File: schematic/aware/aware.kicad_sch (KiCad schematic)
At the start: 28 parts, among them J1 Servo_Conn, J2 Nowcast_LEDS_Conn, J3 Forcast_LEDS_Conn, J4 Battery_Conn, Q1 BC548, U1 Solar_Charger, U2 LM393

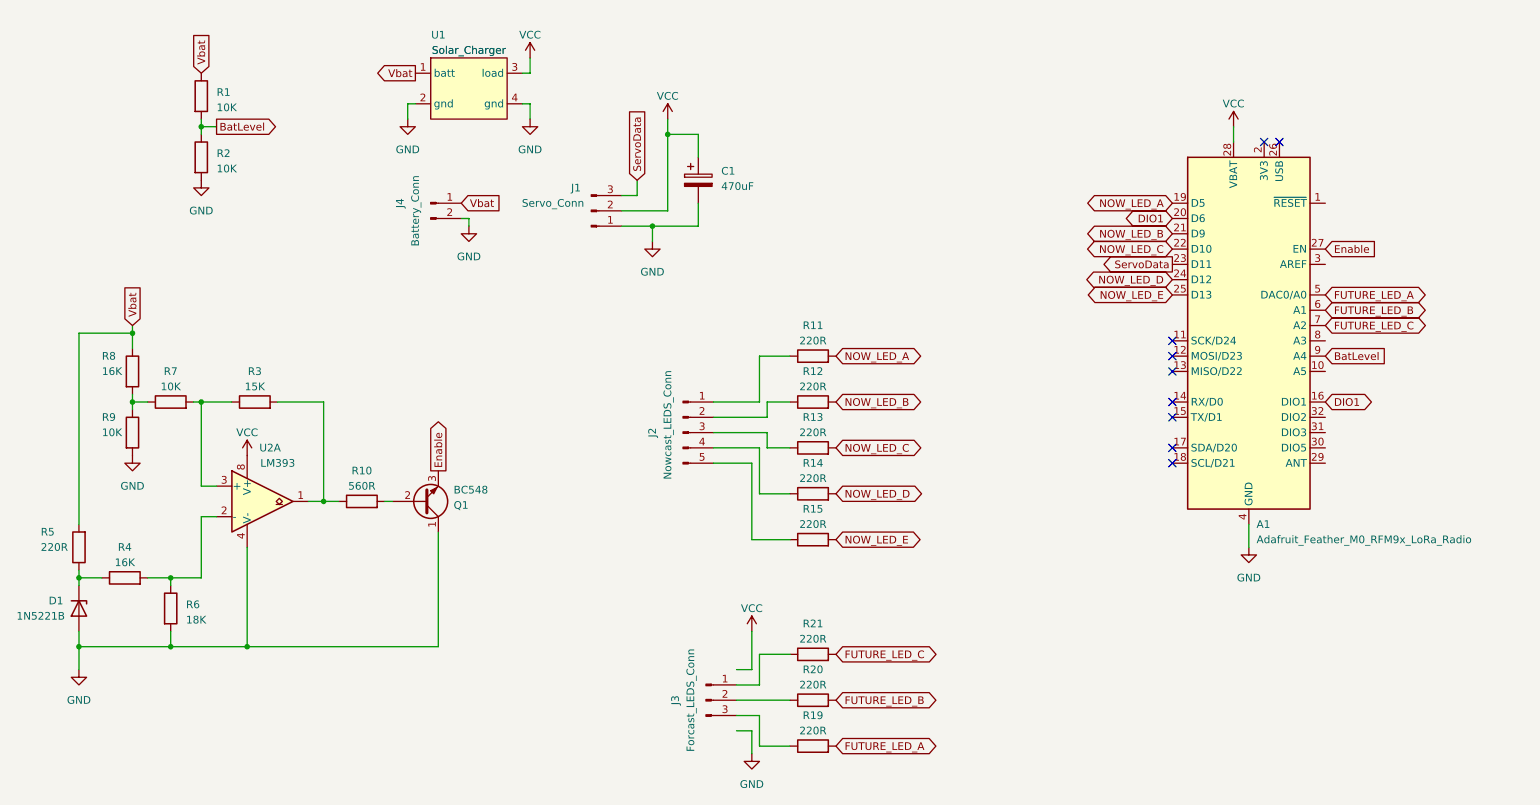
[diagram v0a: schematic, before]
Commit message: adjusted pinout of forcast connector on mainboard
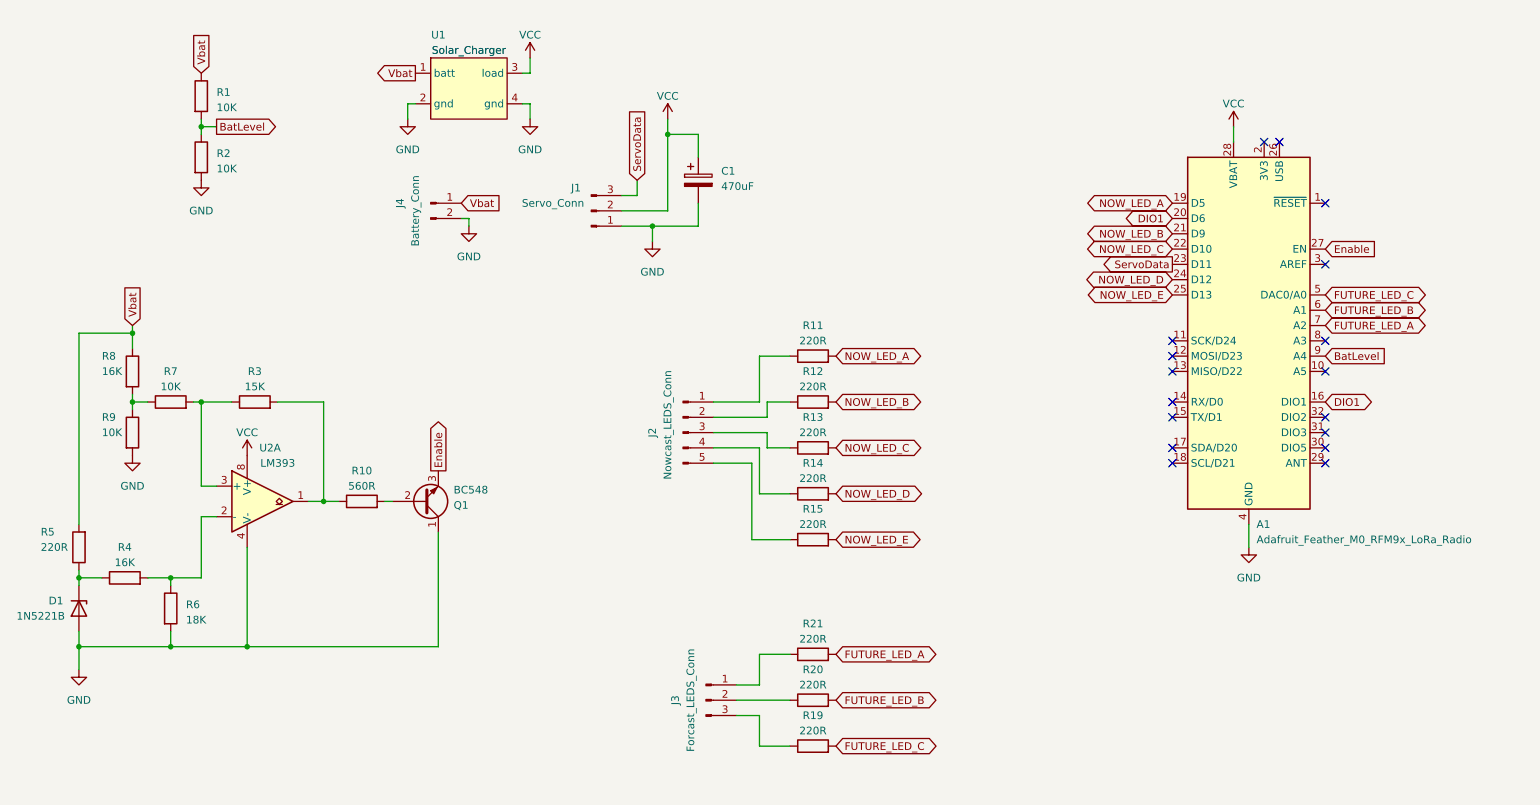
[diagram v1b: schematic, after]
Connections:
- net FUTURE_LED_A: now also A1.7 (A2), R21.2; no longer A1.5 (DAC0/A0), R19.2
- net FUTURE_LED_C: now also A1.5 (DAC0/A0), R19.2; no longer A1.7 (A2), R21.2
- no-connect marks 9 -> 17
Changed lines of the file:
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@@
   (no_connect (at 238.76 43.18))
   (no_connect (at 220.98 88.9))
+  (no_connect (at 246.38 53.34))
   (no_connect (at 236.22 43.18))
+  (no_connect (at 246.38 91.44))
+  (no_connect (at 246.38 96.52))
+  (no_connect (at 246.38 76.2))
   (no_connect (at 220.98 76.2))
   (no_connect (at 220.98 93.98))
   (no_connect (at 220.98 78.74))
+  (no_connect (at 246.38 93.98))
+  (no_connect (at 246.38 88.9))
   (no_connect (at 220.98 81.28))
+  (no_connect (at 246.38 81.28))
+  (no_connect (at 246.38 63.5))
   (wire (pts (xy 142.24 53.34) (xy 142.24 57.15))
     (stroke (width 0) (type default))
@@
     (stroke (width 0) (type default))
   )
-  (wire (pts (xy 151.13 130.81) (xy 151.13 124.46))
-    (stroke (width 0) (type default))
-  )
   (wire (pts (xy 54.61 124.46) (xy 54.61 127))
     (stroke (width 0) (type default))
@@
     (stroke (width 0) (type default))
   )
-  (wire (pts (xy 148.59 140.97) (xy 151.13 140.97))
-    (stroke (width 0) (type default))
-  )
   (wire (pts (xy 80.01 86.36) (xy 80.01 102.87))
     (stroke (width 0) (type default))
@@
     (stroke (width 0) (type default))
   )
-  (wire (pts (xy 148.59 130.81) (xy 151.13 130.81))
-    (stroke (width 0) (type default))
-  )
   (wire (pts (xy 48.26 74.93) (xy 48.26 77.47))
     (stroke (width 0) (type default))
@@
   )
   (wire (pts (xy 54.61 115.57) (xy 59.69 115.57))
-    (stroke (width 0) (type default))
-  )
-  (wire (pts (xy 151.13 140.97) (xy 151.13 144.78))
     (stroke (width 0) (type default))
   )
@@
     )
   )
-  (global_label "FUTURE_LED_A" (shape bidirectional) (at 165.1 143.51 0) (fields_autoplaced)
-    (effects (font (size 1.27 1.27)) (justify left))
-    (property "Intersheetrefs" "${INTERSHEET_REFS}" (at 181.9112 143.51 0)
-      (effects (font (size 1.27 1.27)) (justify left) hide)
-    )
-  )
-  (global_label "FUTURE_LED_A" (shape bidirectional) (at 246.38 68.58 0) (fields_autoplaced)
-    (effects (font (size 1.27 1.27)) (justify left))
-    (property "Intersheetrefs" "${INTERSHEET_REFS}" (at 263.1912 68.58 0)
+  (global_label "FUTURE_LED_A" (shape bidirectional) (at 165.1 128.27 0) (fields_autoplaced)
+    (effects (font (size 1.27 1.27)) (justify left))
+    (property "Intersheetrefs" "${INTERSHEET_REFS}" (at 181.9112 128.27 0)
+      (effects (font (size 1.27 1.27)) (justify left) hide)
+    )
+  )
+  (global_label "FUTURE_LED_A" (shape bidirectional) (at 246.38 73.66 0) (fields_autoplaced)
+    (effects (font (size 1.27 1.27)) (justify left))
+    (property "Intersheetrefs" "${INTERSHEET_REFS}" (at 263.1912 73.66 0)
       (effects (font (size 1.27 1.27)) (justify left) hide)
     )
@@
     )
   )
-  (global_label "FUTURE_LED_C" (shape bidirectional) (at 246.38 73.66 0) (fields_autoplaced)
-    (effects (font (size 1.27 1.27)) (justify left))
-    (property "Intersheetrefs" "${INTERSHEET_REFS}" (at 263.3726 73.66 0)
+  (global_label "FUTURE_LED_C" (shape bidirectional) (at 246.38 68.58 0) (fields_autoplaced)
+    (effects (font (size 1.27 1.27)) (justify left))
+    (property "Intersheetrefs" "${INTERSHEET_REFS}" (at 263.3726 68.58 0)
       (effects (font (size 1.27 1.27)) (justify left) hide)
     )
@@
     )
   )
-  (global_label "FUTURE_LED_C" (shape bidirectional) (at 165.1 128.27 0) (fields_autoplaced)
-    (effects (font (size 1.27 1.27)) (justify left))
-    (property "Intersheetrefs" "${INTERSHEET_REFS}" (at 182.0926 128.27 0)
+  (global_label "FUTURE_LED_C" (shape bidirectional) (at 165.1 143.51 0) (fields_autoplaced)
+    (effects (font (size 1.27 1.27)) (justify left))
+    (property "Intersheetrefs" "${INTERSHEET_REFS}" (at 182.0926 143.51 0)
       (effects (font (size 1.27 1.27)) (justify left) hide)
     )
@@
     )
   )
-  (symbol (lib_id "power:VCC") (at 151.13 124.46 0) (mirror y) (unit 1)
-    (in_bom yes) (on_board yes) (dnp no) (fields_autoplaced)
-    (property "Reference" "#PWR016" (at 151.13 128.27 0)
-      (effects (font (size 1.27 1.27)) hide)
-    )
-    (property "Value" "VCC" (at 151.13 120.65 0)
-      (effects (font (size 1.27 1.27)))
-    )
-    (property "Footprint" "" (at 151.13 124.46 0)
-      (effects (font (size 1.27 1.27)) hide)
-    )
-    (property "Datasheet" "" (at 151.13 124.46 0)
-      (effects (font (size 1.27 1.27)) hide)
-    )
-    (pin "1")
-    (instances
-      (project "aware"
-        (path "/99d9840a-219b-493f-8a7c-580d5c4ba78d"
-          (reference "#PWR016") (unit 1)
-        )
-      )
-    )
-  )
   (symbol (lib_id "Device:R") (at 48.26 91.44 0) (unit 1)
     (in_bom yes) (on_board yes) (dnp no)
@@
         )
       )
-    )
-  )
-  (symbol (lib_id "power:GND") (at 151.13 144.78 0) (mirror y) (unit 1)
-    (in_bom yes) (on_board yes) (dnp no) (fields_autoplaced)
-    (property "Reference" "#PWR017" (at 151.13 151.13 0)
-      (effects (font (size 1.27 1.27)) hide)
-    )
-    (property "Value" "GND" (at 151.13 149.86 0)
-      (effects (font (size 1.27 1.27)))
-    )
-    (property "Footprint" "" (at 151.13 144.78 0)
-      (effects (font (size 1.27 1.27)) hide)
-    )
-    (property "Datasheet" "" (at 151.13 144.78 0)
-      (effects (font (size 1.27 1.27)) hide)
-    )
-    (pin "1")
-    (instances
-      (project "aware"
-        (path "/99d9840a-219b-493f-8a7c-580d5c4ba78d"
-          (reference "#PWR017") (unit 1)
-        )
-      )
